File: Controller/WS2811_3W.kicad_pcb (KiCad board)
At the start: 2 copper layers, 40 x 50 mm, 43 parts, among them J1 Conn_01x01_Female, J2 Conn_01x01_Female, J3 Conn_01x01_Female, J4 Conn_01x01_Female, J5 Conn_01x01_Female, J6 Conn_01x01_Female, U1 MAX485E, U2 WS2811, U3 MAX485E, U4 AMS1117-5.0, U5 BP1808, U6 BP1808, U7 BP1808

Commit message: pcb stuff
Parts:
- added J10: Conn_01x01_Female, Connector_Wire:SolderWirePad_1x01_SMD_1x2mm, F.Cu at (93.6, 63.8)
- added J11: Conn_01x01_Female, Connector_Wire:SolderWirePad_1x01_SMD_1x2mm, F.Cu at (100.6, 63.8)
- added J12: Conn_01x01_Female, Connector_Wire:SolderWirePad_1x01_SMD_1x2mm, F.Cu at (102.6, 63.8)
- added J7: Conn_01x01_Female, Connector_Wire:SolderWirePad_1x01_SMD_1x2mm, F.Cu at (82.6, 63.8)
- added J8: Conn_01x01_Female, Connector_Wire:SolderWirePad_1x01_SMD_1x2mm, F.Cu at (84.6, 63.8)
- added J9: Conn_01x01_Female, Connector_Wire:SolderWirePad_1x01_SMD_1x2mm, F.Cu at (91.6, 63.8)
- added R6: 10k, Resistor_SMD:R_0603_1608Metric, F.Cu at (105.8, 86.0)
- added R7: 10k, Resistor_SMD:R_0603_1608Metric, F.Cu at (106.5, 84.4)
- added R8: 10k, Resistor_SMD:R_0603_1608Metric, F.Cu at (101.9, 89.8)
- D4, D5, D6: footprint Diode_SMD:D_SMA -> Diode_SMD:D_SOD-123F
- moved C4 184.1 mm to (73.9, 69.1), turned to 90 degrees
- moved C6 174.7 mm to (83.2, 72.1), turned to -90 degrees
- moved C11 171.4 mm to (85.0, 72.0), turned to -90 degrees
- moved R4 168.5 mm to (83.6, 67.9), turned to 90 degrees
- moved U5 166.2 mm to (78.5, 70.6)
- moved C7 166.0 mm to (85.7, 67.1), turned to -90 degrees
- moved L1 163.5 mm to (89.2, 68.1), turned to 90 degrees
- moved C10 156.4 mm to (78.5, 99.3), turned to 90 degrees
- moved D4 156.0 mm to (88.9, 72.7)
- moved J5 148.8 mm to (81.2, 108.9), turned to 180 degrees
- moved C8 135.1 mm to (83.4, 104.4)
- moved C12 133.2 mm to (77.1, 78.2), turned to 180 degrees
- moved C13 132.6 mm to (76.1, 87.6), turned to 180 degrees
- moved C14 131.1 mm to (76.3, 89.5), turned to 180 degrees
- moved J3 130.6 mm to (95.2, 108.9)
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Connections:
- net B+ renamed /DCDC_CC2/OUT+
- net B- renamed /DCDC_CC2/OUT-
- net G+ renamed /DCDC_CC1/OUT+
- net G- renamed /DCDC_CC1/OUT-
- net R+ renamed /DCDC_CC/OUT+
- net R- renamed /DCDC_CC/OUT-
- U1 pad 1: WS_DIN -> unconnected-(U1-Pad1)
- U1 pad 2: GND -> unconnected-(U1-Pad2)
- U1 pad 3: GND -> unconnected-(U1-Pad3)
- U1 pad 5: GND -> unconnected-(U1-Pad5)
- U1 pad 6: Net-(J2-Pad1) -> unconnected-(U1-Pad6)
- U1 pad 7: Net-(J1-Pad1) -> unconnected-(U1-Pad7)
- U1 pad 8: +5V -> unconnected-(U1-Pad8)
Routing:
- net +5V: track 0.00 -> 84.8 mm
- net DIM_R: track 0.00 -> 43.6 mm, vias 0 -> 2
- net DIM_G: track 0.00 -> 39.4 mm, vias 0 -> 2
- net /DCDC_CC1/OUT-: track 0.00 -> 31.3 mm
- net /DCDC_CC1/OUT+: track 0.00 -> 26.7 mm
- net GND: track 0.00 -> 24.9 mm, vias 0 -> 33
- net DIM_B: track 0.00 -> 24.3 mm
- net WS_DO: track 0.00 -> 20.4 mm
- net WS_DIN: track 0.00 -> 14.4 mm
- net Net-(J4-Pad1): track 0.00 -> 5.99 mm
- net Net-(J3-Pad1): track 0.00 -> 5.92 mm
- net Net-(J2-Pad1): track 0.00 -> 5.90 mm
- net Net-(J1-Pad1): track 0.00 -> 5.86 mm
- net Net-(C16-Pad1): track 0.00 -> 5.49 mm
- net unconnected-(U1-Pad3): track 0.00 -> 4.01 mm
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- added copper zone on F.Cu, net /DCDC_CC/OUT+
- added copper zone on F.Cu, net /DCDC_CC/OUT-
- added copper zone on F.Cu, net /DCDC_CC1/OUT+
- added copper zone on F.Cu, net /DCDC_CC1/OUT-
- added copper zone on F.Cu, net /DCDC_CC2/OUT+
- added copper zone on F.Cu, net /DCDC_CC2/OUT-
- added copper zone on B.Cu, net GND
- added copper zone on F.Cu, net GND
- added copper zone on F.Cu, net Net-(D4-Pad2)
- added copper zone on F.Cu, net Net-(D5-Pad2)
- added copper zone on F.Cu, net Net-(D6-Pad2)
- added copper zone on B.Cu, net VCC
- added copper zone on F.Cu, net VCC

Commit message: finish PCB
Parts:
- added G***: LOGO, Techbeard:Techbeard_6x6, F.Cu at (84.8, 77.8)
- J5, J6: footprint Connector_Wire:SolderWirePad_1x01_SMD_1x2mm -> Techbeard:SolderWirePad_1x01_SMD_2x4mm
- moved J6 0.38 mm to (84.5, 109.2)
- moved J5 0.24 mm to (81.1, 109.1)
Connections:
- U1 pad 1: unconnected-(U1-Pad1) -> WS_DIN
- U1 pad 2: unconnected-(U1-Pad2) -> GND
- U1 pad 3: unconnected-(U1-Pad3) -> GND
- U1 pad 5: unconnected-(U1-Pad5) -> GND
- U1 pad 6: unconnected-(U1-Pad6) -> Net-(J2-Pad1)
- U1 pad 7: unconnected-(U1-Pad7) -> Net-(J1-Pad1)
- U1 pad 8: unconnected-(U1-Pad8) -> +5V
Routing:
- net GND: track 24.9 -> 31.0 mm, vias 33 -> 39
- net unconnected-(U1-Pad3): track 4.01 -> 0.00 mm
- net VCC: vias 15 -> 16
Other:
- board text added: "B+"
- board text added: "B-"
- board text added: "G+"
- board text added: "G-"
- board text added: "GND"
- board text added: "IN"
- board text added: "OUT"
- board text added: "R+"
- board text added: "R-"
- board text added: "Vcc"

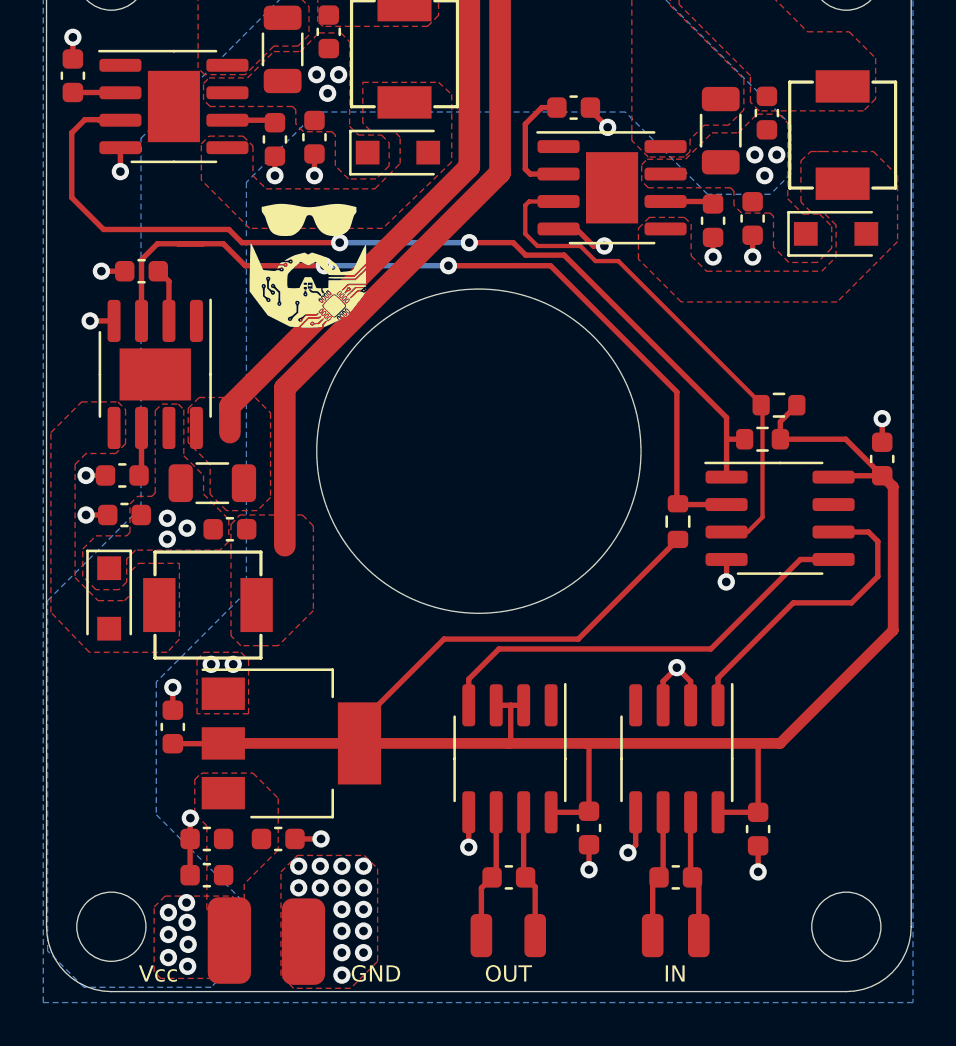
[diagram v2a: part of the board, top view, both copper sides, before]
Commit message: switch to different LDO
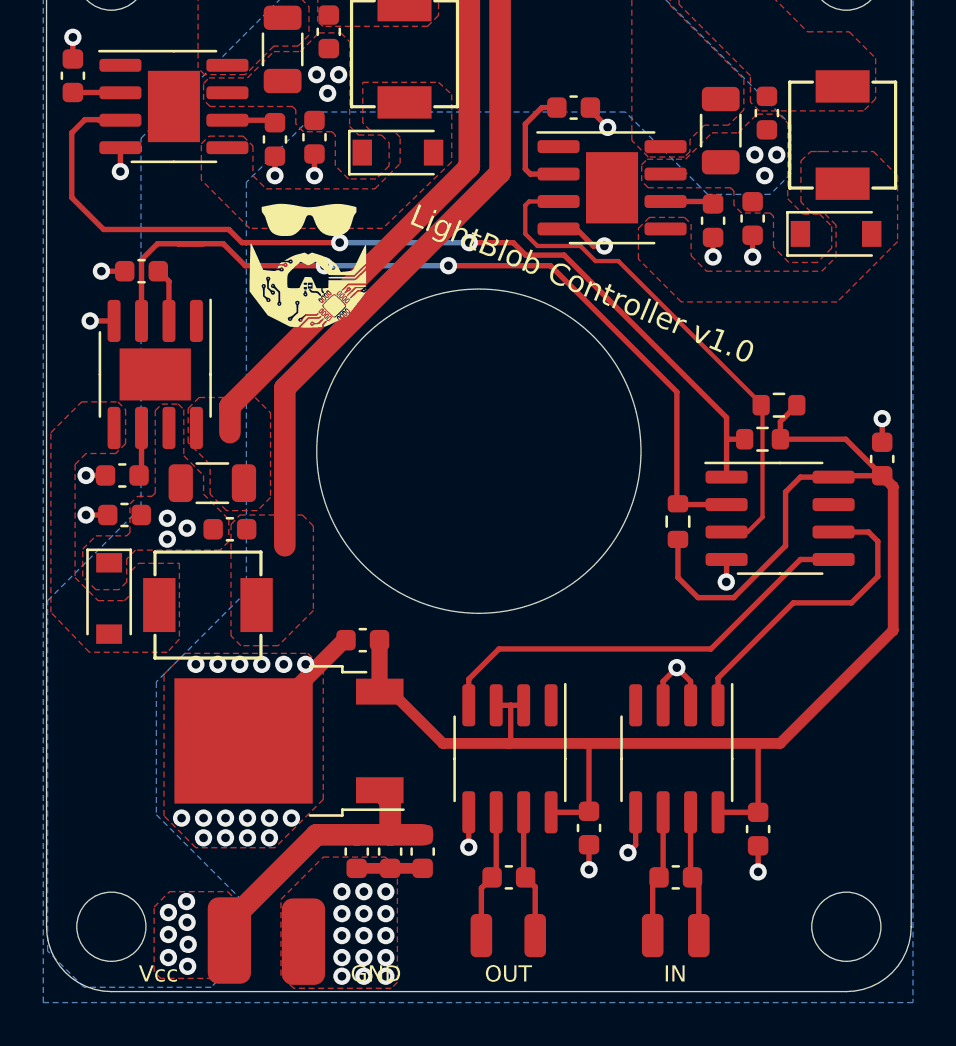
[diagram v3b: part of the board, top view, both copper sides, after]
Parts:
- C1, C10, C3: value 100nF -> 100n
- D4, D5, D6: value D_Schottky -> 40V 1A; footprint Diode_SMD:D_SOD-123F -> Diode_SMD:D_SOD-123
- J10: value Conn_01x01_Female -> G-
- J11: value Conn_01x01_Female -> B+
- J12: value Conn_01x01_Female -> B-
- J5: value Conn_01x01_Female -> 12V
- J6: value Conn_01x01_Female -> GND
- J7: value Conn_01x01_Female -> R+
- J8: value Conn_01x01_Female -> R-
- J9: value Conn_01x01_Female -> G+
- R3, R4, R5: value R -> 0R68
- U4: value AMS1117-5.0 -> LM78M05_TO252; footprint Package_TO_SOT_SMD:SOT-223-3_TabPin2 -> Package_TO_SOT_SMD:TO-252-2
- moved C9 10.0 mm to (90.0, 105.0), turned to -90 degrees
- moved C10 9.66 mm to (87.3, 95.2), turned to 180 degrees
- moved C5 6.96 mm to (87.0, 105.0), turned to -90 degrees
- moved C8 5.21 mm to (88.5, 105.0), turned to -90 degrees
- moved U4 0.16 mm to (83.9, 99.9), turned to 180 degrees
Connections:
- U4 pad 1: GND -> VCC
- U4 pad 2: +5V -> GND
- U4 pad 3: VCC -> +5V
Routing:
- net VCC: track 0.00 -> 13.7 mm
- net +5V: track 84.8 -> 72.5 mm
- net GND: track 31.0 -> 35.7 mm, vias 39 -> 50
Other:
- board text added: "LightBlob Controller v1.0"

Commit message: generate fabrication files
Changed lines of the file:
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@@
       (layerselection 0x00010fc_ffffffff)
       (disableapertmacros false)
-      (usegerberextensions false)
+      (usegerberextensions true)
       (usegerberattributes true)
       (usegerberadvancedattributes true)
-      (creategerberjobfile true)
+      (creategerberjobfile false)
       (svguseinch false)
       (svgprecision 6)
@@
       (outputformat 1)
       (mirror false)
-      (drillshape 1)
+      (drillshape 0)
       (scaleselection 1)
-      (outputdirectory "")
+      (outputdirectory "gerber/")
     )
   )
@@
     (fp_line (start -1.6 0.8) (end -1.6 -0.8) (layer "F.Fab") (width 0.1))
     (fp_line (start 1.6 0.8) (end -1.6 0.8) (layer "F.Fab") (width 0.1))
-    (pad "1" smd roundrect locked (at -1.4625 0) (size 1.125 1.75) (layers "F.Cu" "F.Paste" "F.Mask") (roundrect_rratio 0.222222)
+    (pad "1" smd roundrect locked (at -1.4625 0) (size 1.125 1.75) (layers "F.Cu" "F.Paste" "F.Mask") (roundrect_rratio 0.2222222222)
       (net 4 "VCC") (pintype "passive"))
-    (pad "2" smd roundrect locked (at 1.4625 0) (size 1.125 1.75) (layers "F.Cu" "F.Paste" "F.Mask") (roundrect_rratio 0.222222)
+    (pad "2" smd roundrect locked (at 1.4625 0) (size 1.125 1.75) (layers "F.Cu" "F.Paste" "F.Mask") (roundrect_rratio 0.2222222222)
       (net 14 "/DCDC_CC1/OUT+") (pintype "passive"))
     (model "${KICAD6_3DMODEL_DIR}/Resistor_SMD.3dshapes/R_1206_3216Metric.wrl"
@@
     (fp_line (start 1.6 0.8) (end -1.6 0.8) (layer "F.Fab") (width 0.1))
     (fp_line (start -1.6 -0.8) (end 1.6 -0.8) (layer "F.Fab") (width 0.1))
-    (pad "1" smd roundrect locked (at -1.4625 0 90) (size 1.125 1.75) (layers "F.Cu" "F.Paste" "F.Mask") (roundrect_rratio 0.222222)
+    (pad "1" smd roundrect locked (at -1.4625 0 90) (size 1.125 1.75) (layers "F.Cu" "F.Paste" "F.Mask") (roundrect_rratio 0.2222222222)
       (net 4 "VCC") (pintype "passive"))
-    (pad "2" smd roundrect locked (at 1.4625 0 90) (size 1.125 1.75) (layers "F.Cu" "F.Paste" "F.Mask") (roundrect_rratio 0.222222)
+    (pad "2" smd roundrect locked (at 1.4625 0 90) (size 1.125 1.75) (layers "F.Cu" "F.Paste" "F.Mask") (roundrect_rratio 0.2222222222)
       (net 15 "/DCDC_CC2/OUT+") (pintype "passive"))
     (model "${KICAD6_3DMODEL_DIR}/Resistor_SMD.3dshapes/R_1206_3216Metric.wrl"
@@
     (fp_line (start 1.6 0.8) (end -1.6 0.8) (layer "F.Fab") (width 0.1))
     (fp_line (start 1.6 -0.8) (end 1.6 0.8) (layer "F.Fab") (width 0.1))
-    (pad "1" smd roundrect locked (at -1.4625 0 90) (size 1.125 1.75) (layers "F.Cu" "F.Paste" "F.Mask") (roundrect_rratio 0.222222)
+    (pad "1" smd roundrect locked (at -1.4625 0 90) (size 1.125 1.75) (layers "F.Cu" "F.Paste" "F.Mask") (roundrect_rratio 0.2222222222)
       (net 4 "VCC") (pintype "passive"))
-    (pad "2" smd roundrect locked (at 1.4625 0 90) (size 1.125 1.75) (layers "F.Cu" "F.Paste" "F.Mask") (roundrect_rratio 0.222222)
+    (pad "2" smd roundrect locked (at 1.4625 0 90) (size 1.125 1.75) (layers "F.Cu" "F.Paste" "F.Mask") (roundrect_rratio 0.2222222222)
       (net 13 "/DCDC_CC/OUT+") (pintype "passive"))
     (model "${KICAD6_3DMODEL_DIR}/Resistor_SMD.3dshapes/R_1206_3216Metric.wrl"
